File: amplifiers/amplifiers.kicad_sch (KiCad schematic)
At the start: 4 parts, among them J1 Conn_01x03_Pin, J2 Conn_01x02_Pin, J3 Conn_01x03_Pin, U1 ADA4898-2

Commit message: Finishes version 0.1 of amplifier module board
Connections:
- net at J3.2 (Pin_2): now also U1.6 (-); no longer U1.5 (+)
- net at J3.3 (Pin_3): now also U1.5 (+); no longer U1.6 (-)
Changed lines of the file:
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@@
     )
   )
-  (symbol (lib_id "Amplifier_Operational:ADA4898-2") (at 64.77 86.36 0) (unit 2)
-    (in_bom yes) (on_board yes) (dnp no) (fields_autoplaced)
-    (property "Reference" "U1" (at 64.77 76.2 0)
+  (symbol (lib_id "Amplifier_Operational:ADA4898-2") (at 64.77 86.36 0) (mirror x) (unit 2)
+    (in_bom yes) (on_board yes) (dnp no)
+    (property "Reference" "U1" (at 63.5 80.01 0)
       (effects (font (size 1.27 1.27)))
     )
-    (property "Value" "ADA4898-2" (at 64.77 78.74 0)
+    (property "Value" "ADA4898-2" (at 64.77 77.47 0)
       (effects (font (size 1.27 1.27)))
     )
-    (property "Footprint" "Package_SO:SOIC-8-1EP_3.9x4.9mm_P1.27mm_EP2.41x3.81mm" (at 63.5 93.98 0)
+    (property "Footprint" "Package_SO:SOIC-8-1EP_3.9x4.9mm_P1.27mm_EP2.41x3.81mm" (at 63.5 78.74 0)
       (effects (font (size 1.27 1.27)) hide)
     )

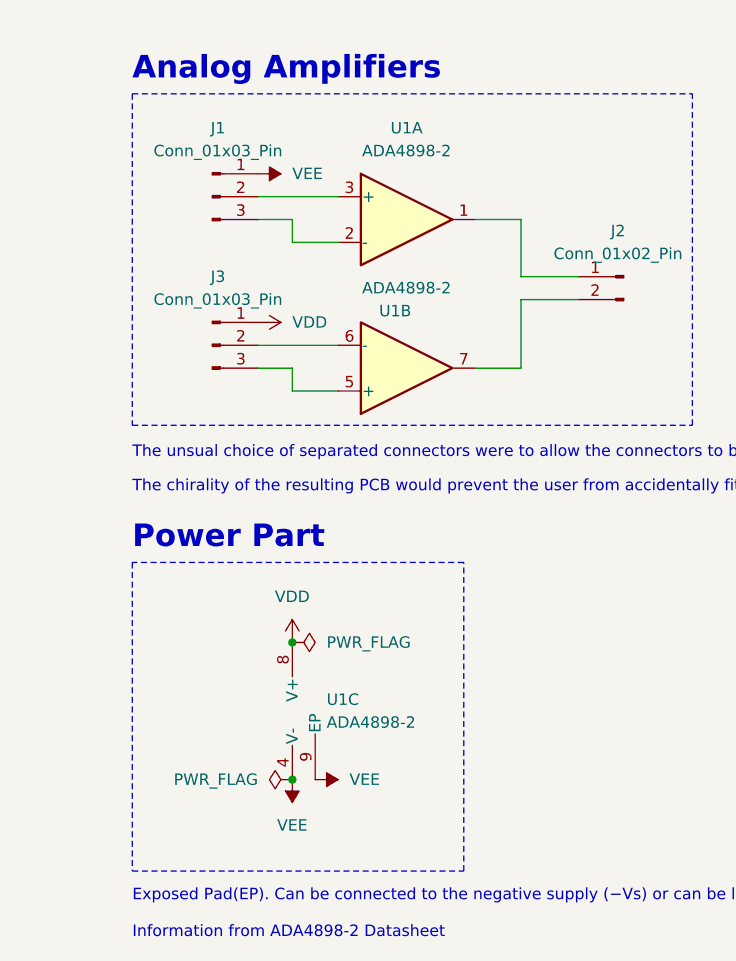
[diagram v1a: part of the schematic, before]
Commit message: Modifies auxiliary boards
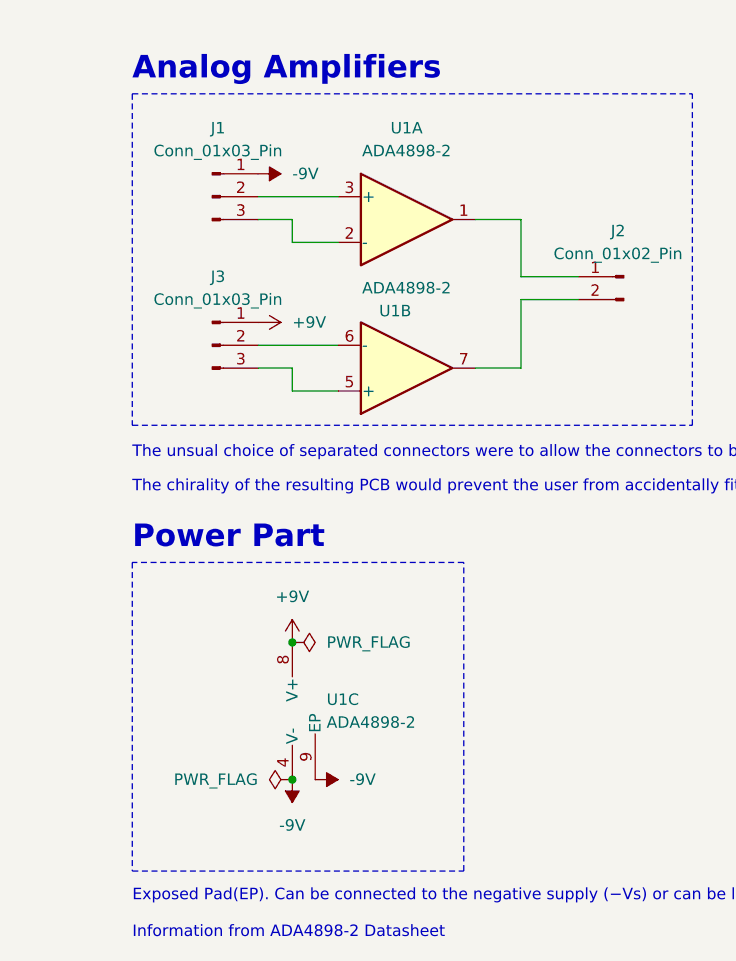
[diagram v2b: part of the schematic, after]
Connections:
- net VDD renamed +9V
- net VEE renamed -9V
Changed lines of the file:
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@@
     (comment 1 "Part of the Project Einstein-Boltzmann")
   )
+  (junction (at 52.07 116.84) (diameter 0) (color 0 0 0 0)
+  )
   (junction (at 52.07 132.08) (diameter 0) (color 0 0 0 0)
-  )
-  (junction (at 52.07 116.84) (diameter 0) (color 0 0 0 0)
   )
   (wire (pts (xy 52.07 86.36) (xy 52.07 88.9))
@@
         (path "/669b9592-25f7-470c-839f-88d0350141e7"
           (reference "J1") (unit 1)
-        )
-      )
-    )
-  )
-  (symbol (lib_id "power:VDD") (at 52.07 116.84 0) (unit 1)
-    (in_bom yes) (on_board yes) (dnp no) (fields_autoplaced)
-    (property "Reference" "#PWR05" (at 52.07 120.65 0)
-      (effects (font (size 1.27 1.27)) hide)
-    )
-    (property "Value" "VDD" (at 52.07 111.76 0)
-      (effects (font (size 1.27 1.27)))
-    )
-    (property "Footprint" "" (at 52.07 116.84 0)
-      (effects (font (size 1.27 1.27)) hide)
-    )
-    (property "Datasheet" "" (at 52.07 116.84 0)
-      (effects (font (size 1.27 1.27)) hide)
-    )
-    (pin "1")
-    (instances
-      (project "amplifiers"
-        (path "/669b9592-25f7-470c-839f-88d0350141e7"
-          (reference "#PWR05") (unit 1)
         )
       )
@@
     )
   )
-  (symbol (lib_id "power:VEE") (at 48.26 64.77 270) (unit 1)
-    (in_bom yes) (on_board yes) (dnp no) (fields_autoplaced)
-    (property "Reference" "#PWR04" (at 44.45 64.77 0)
-      (effects (font (size 1.27 1.27)) hide)
-    )
-    (property "Value" "VEE" (at 52.07 64.77 90)
-      (effects (font (size 1.27 1.27)) (justify left))
-    )
-    (property "Footprint" "" (at 48.26 64.77 0)
-      (effects (font (size 1.27 1.27)) hide)
-    )
-    (property "Datasheet" "" (at 48.26 64.77 0)
-      (effects (font (size 1.27 1.27)) hide)
-    )
-    (pin "1")
-    (instances
-      (project "amplifiers"
-        (path "/669b9592-25f7-470c-839f-88d0350141e7"
-          (reference "#PWR04") (unit 1)
-        )
-      )
-    )
-  )
-  (symbol (lib_id "power:VDD") (at 48.26 81.28 270) (unit 1)
-    (in_bom yes) (on_board yes) (dnp no) (fields_autoplaced)
-    (property "Reference" "#PWR03" (at 44.45 81.28 0)
-      (effects (font (size 1.27 1.27)) hide)
-    )
-    (property "Value" "VDD" (at 52.07 81.28 90)
-      (effects (font (size 1.27 1.27)) (justify left))
-    )
-    (property "Footprint" "" (at 48.26 81.28 0)
-      (effects (font (size 1.27 1.27)) hide)
-    )
-    (property "Datasheet" "" (at 48.26 81.28 0)
-      (effects (font (size 1.27 1.27)) hide)
-    )
-    (pin "1")
-    (instances
-      (project "amplifiers"
-        (path "/669b9592-25f7-470c-839f-88d0350141e7"
-          (reference "#PWR03") (unit 1)
-        )
-      )
-    )
-  )
   (symbol (lib_id "Amplifier_Operational:ADA4898-2") (at 64.77 69.85 0) (unit 1)
     (in_bom yes) (on_board yes) (dnp no)
@@
     )
   )
-  (symbol (lib_id "power:VEE") (at 52.07 132.08 180) (unit 1)
-    (in_bom yes) (on_board yes) (dnp no) (fields_autoplaced)
-    (property "Reference" "#PWR02" (at 52.07 128.27 0)
-      (effects (font (size 1.27 1.27)) hide)
-    )
-    (property "Value" "VEE" (at 52.07 137.16 0)
-      (effects (font (size 1.27 1.27)))
-    )
-    (property "Footprint" "" (at 52.07 132.08 0)
-      (effects (font (size 1.27 1.27)) hide)
-    )
-    (property "Datasheet" "" (at 52.07 132.08 0)
-      (effects (font (size 1.27 1.27)) hide)
-    )
-    (pin "1")
-    (instances
-      (project "amplifiers"
-        (path "/669b9592-25f7-470c-839f-88d0350141e7"
-          (reference "#PWR02") (unit 1)
-        )
-      )
-    )
-  )
-  (symbol (lib_id "power:VEE") (at 54.61 132.08 270) (unit 1)
-    (in_bom yes) (on_board yes) (dnp no) (fields_autoplaced)
-    (property "Reference" "#PWR01" (at 50.8 132.08 0)
-      (effects (font (size 1.27 1.27)) hide)
-    )
-    (property "Value" "VEE" (at 58.42 132.08 90)
-      (effects (font (size 1.27 1.27)) (justify left))
-    )
-    (property "Footprint" "" (at 54.61 132.08 0)
-      (effects (font (size 1.27 1.27)) hide)
-    )
-    (property "Datasheet" "" (at 54.61 132.08 0)
-      (effects (font (size 1.27 1.27)) hide)
-    )
-    (pin "1")
-    (instances
-      (project "amplifiers"
-        (path "/669b9592-25f7-470c-839f-88d0350141e7"
-          (reference "#PWR01") (unit 1)
+  (symbol (lib_id "power:+9V") (at 48.26 81.28 270) (unit 1)
+    (in_bom yes) (on_board yes) (dnp no) (fields_autoplaced)
+    (property "Reference" "#PWR03" (at 44.45 81.28 0)
+      (effects (font (size 1.27 1.27)) hide)
+    )
+    (property "Value" "+9V" (at 52.07 81.28 90)
+      (effects (font (size 1.27 1.27)) (justify left))
+    )
+    (property "Footprint" "" (at 48.26 81.28 0)
+      (effects (font (size 1.27 1.27)) hide)
+    )
+    (property "Datasheet" "" (at 48.26 81.28 0)
+      (effects (font (size 1.27 1.27)) hide)
+    )
+    (pin "1")
+    (instances
+      (project "amplifiers"
+        (path "/669b9592-25f7-470c-839f-88d0350141e7"
+          (reference "#PWR03") (unit 1)
         )
       )
@@
     )
   )
+  (symbol (lib_id "power:+9V") (at 52.07 116.84 0) (unit 1)
+    (in_bom yes) (on_board yes) (dnp no) (fields_autoplaced)
+    (property "Reference" "#PWR02" (at 52.07 120.65 0)
+      (effects (font (size 1.27 1.27)) hide)
+    )
+    (property "Value" "+9V" (at 52.07 111.76 0)
+      (effects (font (size 1.27 1.27)))
+    )
+    (property "Footprint" "" (at 52.07 116.84 0)
+      (effects (font (size 1.27 1.27)) hide)
+    )
+    (property "Datasheet" "" (at 52.07 116.84 0)
+      (effects (font (size 1.27 1.27)) hide)
+    )
+    (pin "1")
+    (instances
+      (project "amplifiers"
+        (path "/669b9592-25f7-470c-839f-88d0350141e7"
+          (reference "#PWR02") (unit 1)
+        )
+      )
+    )
+  )
+  (symbol (lib_id "power:-9V") (at 48.26 64.77 270) (unit 1)
+    (in_bom yes) (on_board yes) (dnp no) (fields_autoplaced)
+    (property "Reference" "#PWR04" (at 45.085 64.77 0)
+      (effects (font (size 1.27 1.27)) hide)
+    )
+    (property "Value" "-9V" (at 52.07 64.77 90)
+      (effects (font (size 1.27 1.27)) (justify left))
+    )
+    (property "Footprint" "" (at 48.26 64.77 0)
+      (effects (font (size 1.27 1.27)) hide)
+    )
+    (property "Datasheet" "" (at 48.26 64.77 0)
+      (effects (font (size 1.27 1.27)) hide)
+    )
+    (pin "1")
+    (instances
+      (project "amplifiers"
+        (path "/669b9592-25f7-470c-839f-88d0350141e7"
+          (reference "#PWR04") (unit 1)
+        )
+      )
+    )
+  )
   (symbol (lib_id "power:PWR_FLAG") (at 52.07 116.84 270) (unit 1)
     (in_bom yes) (on_board yes) (dnp no) (fields_autoplaced)
@@
         )
       )
+    )
+  )
+  (symbol (lib_id "power:-9V") (at 54.61 132.08 270) (unit 1)
+    (in_bom yes) (on_board yes) (dnp no) (fields_autoplaced)
+    (property "Reference" "#PWR06" (at 51.435 132.08 0)
+      (effects (font (size 1.27 1.27)) hide)
+    )
+    (property "Value" "-9V" (at 58.42 132.08 90)
+      (effects (font (size 1.27 1.27)) (justify left))
+    )
+    (property "Footprint" "" (at 54.61 132.08 0)
+      (effects (font (size 1.27 1.27)) hide)
+    )
+    (property "Datasheet" "" (at 54.61 132.08 0)
+      (effects (font (size 1.27 1.27)) hide)
+    )
+    (pin "1")
+    (instances
+      (project "amplifiers"
+        (path "/669b9592-25f7-470c-839f-88d0350141e7"
+          (reference "#PWR06") (unit 1)
+        )
+      )
+    )
+  )
+  (symbol (lib_id "power:-9V") (at 52.07 132.08 180) (unit 1)
+    (in_bom yes) (on_board yes) (dnp no) (fields_autoplaced)
+    (property "Reference" "#PWR01" (at 52.07 128.905 0)
+      (effects (font (size 1.27 1.27)) hide)
+    )
+    (property "Value" "-9V" (at 52.07 137.16 0)
+      (effects (font (size 1.27 1.27)))
+    )
+    (property "Footprint" "" (at 52.07 132.08 0)
+      (effects (font (size 1.27 1.27)) hide)
+    )
+    (property "Datasheet" "" (at 52.07 132.08 0)
+      (effects (font (size 1.27 1.27)) hide)
+    )
+    (pin "1")
+    (instances
+      (project "amplifiers"
+        (path "/669b9592-25f7-470c-839f-88d0350141e7"
+          (reference "#PWR01") (unit 1)
+        )
+      )
